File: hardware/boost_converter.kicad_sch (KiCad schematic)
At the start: 12 parts, among them U4 LiPower Module, U5 TPS61200DRC

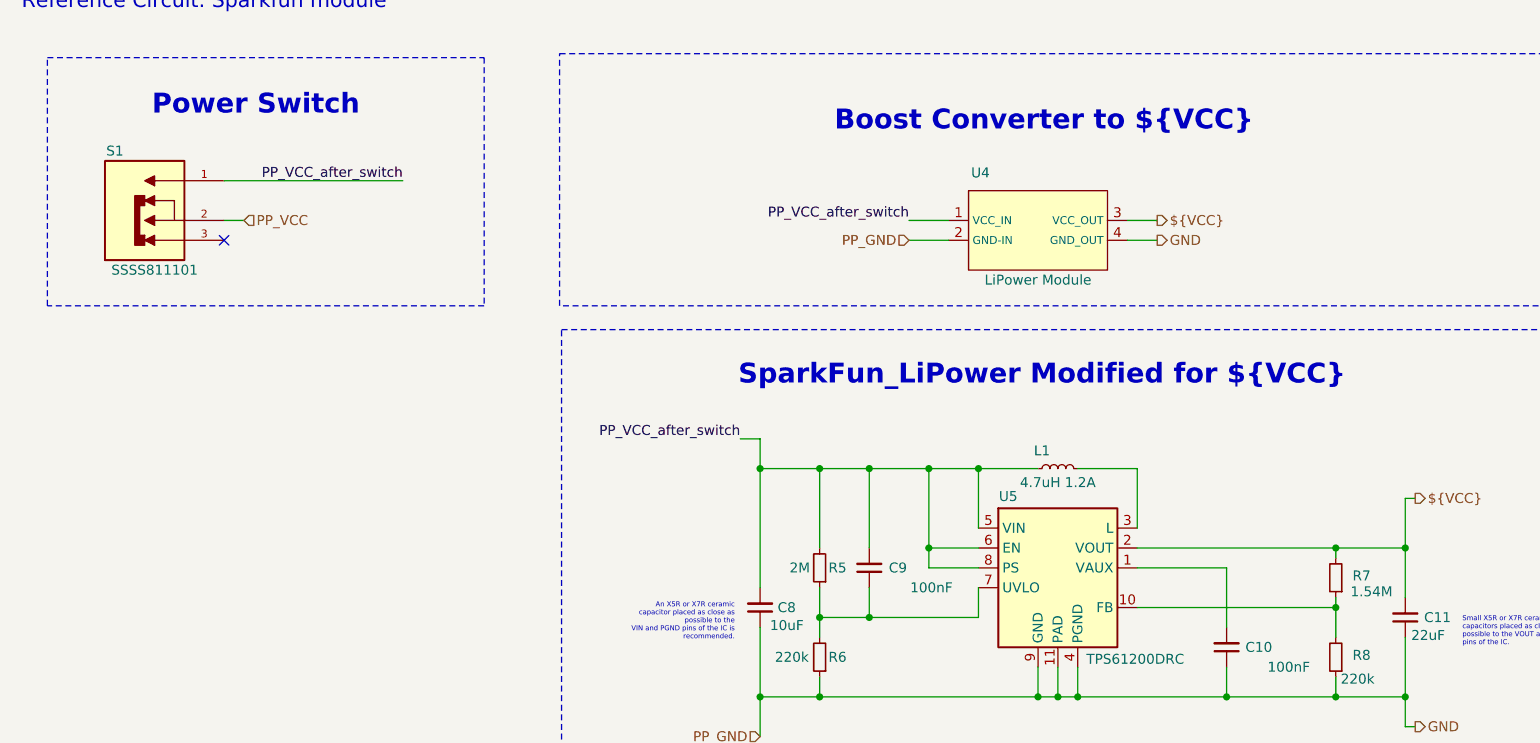
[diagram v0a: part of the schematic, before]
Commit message: Replaced the power switch for a two pin connector. Changed the boost converter design to convert to 5V again. Added a comple files to .gitignore.
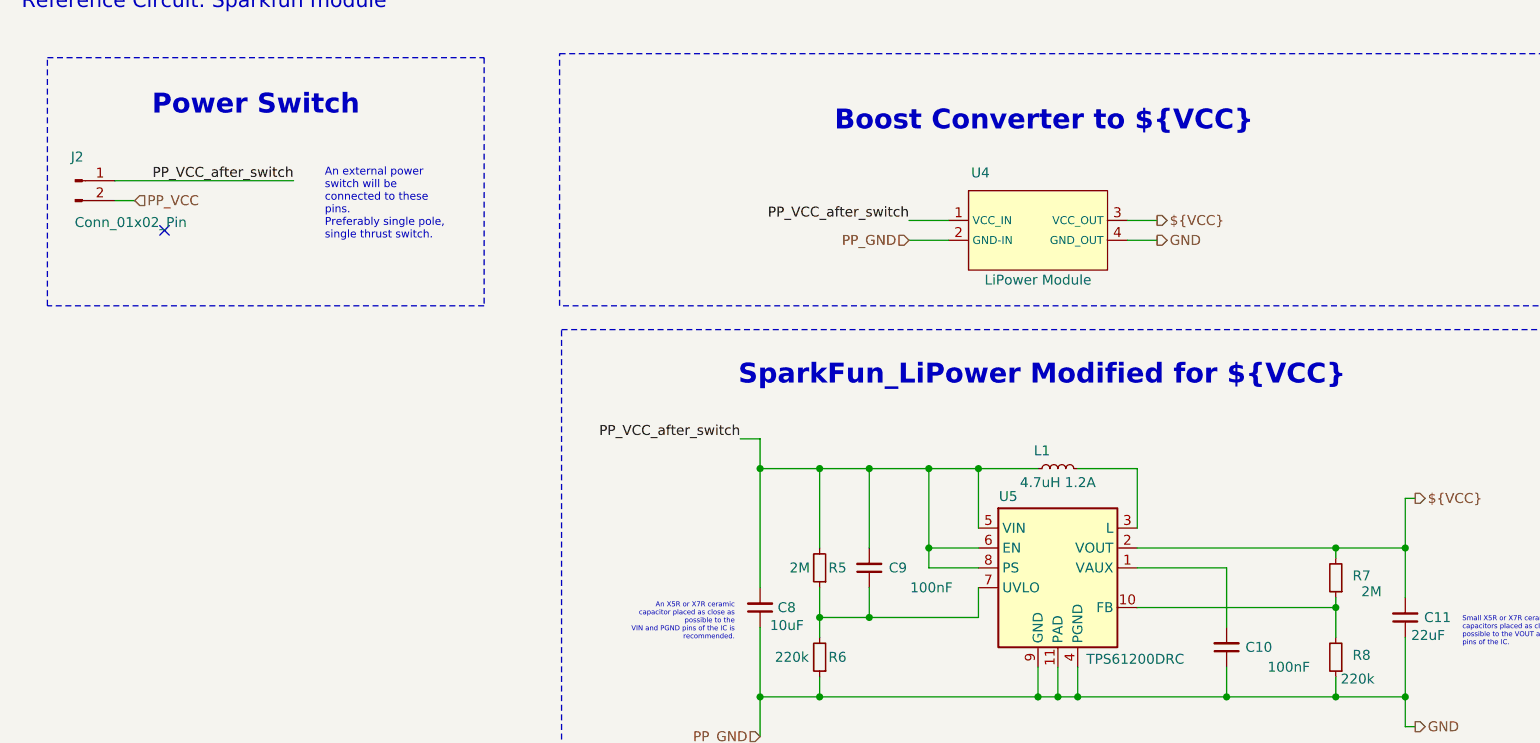
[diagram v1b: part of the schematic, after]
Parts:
- removed S1: SSSS811101, kitchen_timer:SW_SSSS811101, symbol kitchen_timer-symbols_lib:SSSS811101
- added J2: Conn_01x02_Pin, Connector_PinHeader_2.54mm:PinHeader_1x02_P2.54mm_Vertical, symbol Connector:Conn_01x02_Pin
- R7: value 1.54M -> 2M
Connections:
- net PP_VCC: now also J2.2 (Pin_2)
- net PP_VCC_after_switch: now also J2.1 (Pin_1)
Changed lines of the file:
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@@
+		)
+	)
+	(text_box "An external power switch will be connected to these pins.\nPreferably single pole, single thrust switch."
+		(exclude_from_sim no)
+		(at 55.118 74.676 0)
+		(size 19.558 9.906)
+		(margins 0.9525 0.9525 0.9525 0.9525)
+		(stroke
+			(width -0.0001)
+			(type solid)
+		)
+		(fill
+			(type none)
+		)
+		(effects
+			(font
+				(size 1 1)
+			)
+			(justify left top)
 		)
 	)
@@
 	)
 	(no_connect
-		(at 43.18 85.09)
+		(at 35.56 83.82)
 	)
 	(wire
@@
 	(wire
 		(pts
-			(xy 66.04 77.47) (xy 43.18 77.47)
+			(xy 52.07 77.47) (xy 29.21 77.47)
 		)
 		(stroke
@@
 	(wire
 		(pts
-			(xy 45.72 82.55) (xy 43.18 82.55)
+			(xy 31.75 80.01) (xy 29.21 80.01)
 		)
 		(stroke
@@
 	)
 	(label "PP_VCC_after_switch"
-		(at 66.04 77.47 180)
+		(at 52.07 77.47 180)
 		(effects
 			(font
@@
 	(hierarchical_label "PP_VCC"
 		(shape input)
-		(at 45.72 82.55 0)
+		(at 31.75 80.01 0)
 		(effects
 			(font
@@
 	)
 	(symbol
+		(lib_id "Connector:Conn_01x02_Pin")
+		(at 24.13 77.47 0)
+		(unit 1)
+		(exclude_from_sim no)
+		(in_bom yes)
+		(on_board yes)
+		(dnp no)
+		(property "Reference" "J2"
+			(at 24.384 74.422 0)
+			(effects
+				(font
+					(size 1.27 1.27)
+				)
+			)
+		)
+		(property "Value" "Conn_01x02_Pin"
+			(at 31.242 82.804 0)
+			(effects
+				(font
+					(size 1.27 1.27)
+				)
+			)
+		)
+		(property "Footprint" "Connector_PinHeader_2.54mm:PinHeader_1x02_P2.54mm_Vertical"
+			(at 24.13 77.47 0)
+			(effects
+				(font
+					(size 1.27 1.27)
+				)
+				(hide yes)
+			)
+		)
+		(property "Datasheet" "~"
+			(at 24.13 77.47 0)
+			(effects
+				(font
+					(size 1.27 1.27)
+				)
+				(hide yes)
+			)
+		)
+		(property "Description" "Generic connector, single row, 01x02, script generated"
+			(at 24.13 77.47 0)
+			(effects
+				(font
+					(size 1.27 1.27)
+				)
+				(hide yes)
+			)
+		)
+		(property "Supplier Unit Price" "~"
+			(at 24.13 77.47 0)
+			(effects
+				(font
+					(size 1.27 1.27)
+				)
+				(hide yes)
+			)
+		)
+		(property "Part Num" ""
+			(at 24.13 77.47 0)
+			(effects
+				(font
+					(size 1.27 1.27)
+				)
+				(hide yes)
+			)
+		)
+		(property "Package" "~"
+			(at 24.13 77.47 0)
+			(effects
+				(font
+					(size 1.27 1.27)
+				)
+				(hide yes)
+			)
+		)
+		(property "Manuf. Name" "~"
+			(at 24.13 77.47 0)
+			(effects
+				(font
+					(size 1.27 1.27)
+				)
+				(hide yes)
+			)
+		)
+		(property "Manuf. Part #" "~"
+			(at 24.13 77.47 0)
+			(effects
+				(font
+					(size 1.27 1.27)
+				)
+				(hide yes)
+			)
+		)
+		(property "Supplier Name" "~"
+			(at 24.13 77.47 0)
+			(effects
+				(font
+					(size 1.27 1.27)
+				)
+				(hide yes)
+			)
+		)
+		(property "Supplier Part #" "~"
+			(at 24.13 77.47 0)
+			(effects
+				(font
+					(size 1.27 1.27)
+				)
+				(hide yes)
+			)
+		)
+		(property "Supplier Link" "~"
+			(at 24.13 77.47 0)
+			(effects
+				(font
+					(size 1.27 1.27)
+				)
+				(hide yes)
+			)
+		)
+		(pin "1"
+		)
+		(pin "2"
+		)
+		(instances
+			(project ""
+				(path "/8963deea-96bc-4401-b671-98fbe9ed9c6a/8d96c6df-7eb2-480a-982a-3dd8886e54b6"
+					(reference "J2")
+					(unit 1)
+				)
+			)
+		)
+	)
+	(symbol
 		(lib_id "Device:R_Small")
 		(at 119.38 138.43 180)
@@
 				(path "/8963deea-96bc-4401-b671-98fbe9ed9c6a/8d96c6df-7eb2-480a-982a-3dd8886e54b6"
 					(reference "R6")
-					(unit 1)
-				)
-			)
-		)
-	)
-	(symbol
-		(lib_id "kitchen_timer-symbols_lib:SSSS811101")
-		(at 33.02 80.01 0)
-		(unit 1)
-		(exclude_from_sim no)
-		(in_bom yes)
-		(on_board yes)
-		(dnp no)
-		(property "Reference" "S1"
-			(at 29.21 73.66 0)
-			(effects
-				(font
-					(size 1.27 1.27)
-				)
-			)
-		)
-		(property "Value" "SSSS811101"
-			(at 34.29 88.9 0)
-			(effects
-				(font
-					(size 1.27 1.27)
-				)
-			)
-		)
-		(property "Footprint" "kitchen_timer:SW_SSSS811101"
-			(at 33.02 80.01 0)
-			(effects
-				(font
-					(size 1.27 1.27)
-				)
-				(justify bottom)
-				(hide yes)
-			)
-		)
-		(property "Datasheet" "https://jlcpcb.com/api/file/downloadByFileSystemAccessId/8588894528896454656"
-			(at 33.02 80.01 0)
-			(effects
-				(font
-					(size 1.27 1.27)
-				)
-				(hide yes)
-			)
-		)
-		(property "Description" "300mA Horizontal attachment Single Pole Double Throw (SPDT) 5V 10,000 times SMD Slide Switches ROHS"
-			(at 33.02 80.01 0)
-			(effects
-				(font
-					(size 1.27 1.27)
-				)
-				(hide yes)
-			)
-		)
-		(property "Package" "SMD"
-			(at 33.02 80.01 0)
-			(effects
-				(font
-					(size 1.27 1.27)
-				)
-				(justify bottom)
-				(hide yes)
-			)
-		)
-		(property "Manuf. Name" " ALPSALPINE"
-			(at 33.02 80.01 0)
-			(effects
-				(font
-					(size 1.27 1.27)
-				)
-				(hide yes)
-			)
-		)
-		(property "Manuf. Part #" "SSSS811101"
-			(at 33.02 80.01 0)
-			(effects
-				(font
-					(size 1.27 1.27)
-				)
-				(hide yes)
-			)
-		)
-		(property "Supplier Name" "JLCPCB"
-			(at 33.02 80.01 0)
-			(effects
-				(font
-					(size 1.27 1.27)
-				)
-				(hide yes)
-			)
-		)
-		(property "Supplier Part #" "C109335"
-			(at 33.02 80.01 0)
-			(effects
-				(font
-					(size 1.27 1.27)
-				)
-				(hide yes)
-			)
-		)
-		(property "Supplier Link" "https://jlcpcb.com/partdetail/Alpsalpine-SSSS811101/C109335"
-			(at 33.02 80.01 0)
-			(effects
-				(font
-					(size 1.27 1.27)
-				)
-				(hide yes)
-			)
-		)
-		(property "Supplier Unit Price" " $0.1356"
-			(at 33.02 80.01 0)
-			(effects
-				(font
-					(size 1.27 1.27)
-				)
-				(hide yes)
-			)
-		)
-		(pin "2"
-		)
-		(pin "1"
-		)
-		(pin "3"
-		)
-		(instances
-			(project ""
-				(path "/8963deea-96bc-4401-b671-98fbe9ed9c6a/8d96c6df-7eb2-480a-982a-3dd8886e54b6"
-					(reference "S1")
 					(unit 1)
 				)
@@
 			)
 		)
-		(property "Value" "1.54M"
+		(property "Value" "2M"
 			(at 189.992 130.048 0)
 			(effects
@@
 			(at 185.42 128.27 0)
 			(effects
+				(font
+					(size 1.27 1.27)
+				)
+				(hide yes)
+			)
+		)
+		(property "Part Num" ""
+			(at 185.42 128.27 0)
+			(effects

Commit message: Electric Rules Check completed.
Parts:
- added SW3: ~, ~, symbol Switch:SW_SPST
- U4: value LiPower Module -> SparkFun_LiPower
- U5: symbol Regulator_Switching:TPS61200DRC -> kitchen_timer-symbols_lib:TPS61200DRC
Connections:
- net PP_VCC: now also SW3.1 (A); no longer J2.2 (Pin_2)
- new net: J2.2 (Pin_2), SW3.2 (B)
- no-connect marks 1 -> 0
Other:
- moved on the sheet: J2

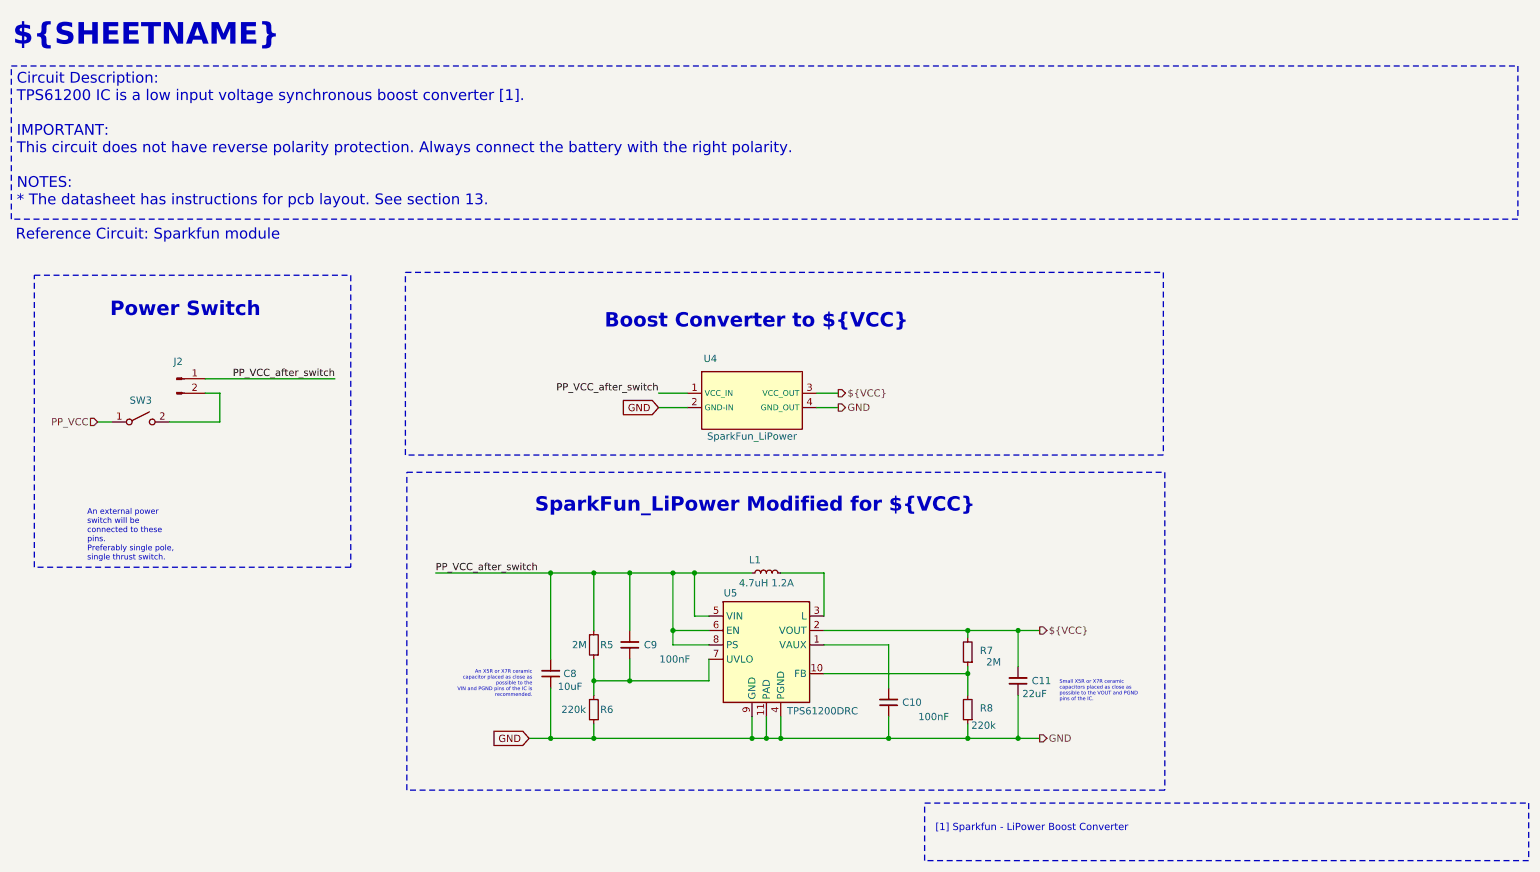
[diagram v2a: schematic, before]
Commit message: Added footprints to mounting holes and selected a part for the test LED.
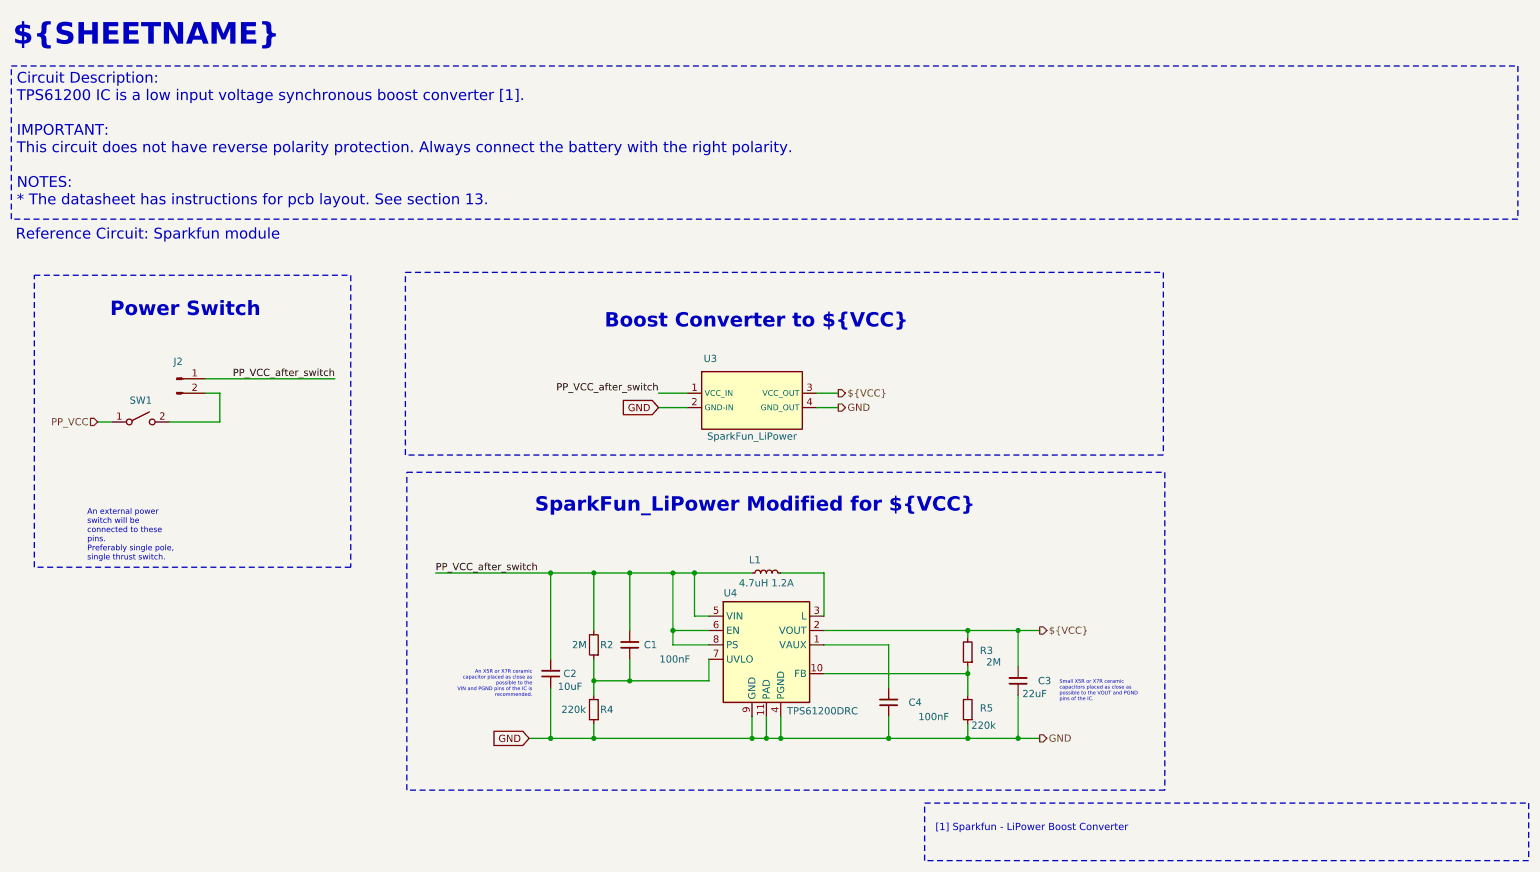
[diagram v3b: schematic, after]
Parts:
- renumbered C9 to C1, C8 to C2, C11 to C3, C10 to C4, R5 to R2, R7 to R3, R6 to R4, R8 to R5, SW3 to SW1, U4 to U3, U5 to U4

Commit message: Made some items DNP and/or Exclude form Board
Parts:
- J2: now left out of the parts list
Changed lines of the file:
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@@
 		(unit 1)
 		(exclude_from_sim no)
-		(in_bom yes)
+		(in_bom no)
 		(on_board yes)
 		(dnp no)
